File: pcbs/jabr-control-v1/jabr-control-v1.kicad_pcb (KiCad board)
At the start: 6 copper layers, 70 x 80 mm, 129 parts, among them J10001 ARJM11D7-502-AB-EW2, J10002 TYPE-C-31-M-12, J4001 MDT275E01001, J401 U.FL-R-SMT-K_895, J402 U.FL-R-SMT-K_895, J6001 MSPE-J2L0-x00, J9001 43045-0201, Q2602 DMN21D2UFB-7B, U1201 TPS259472ARPWR, U1301 MAX20004AFOC/VY+T, U2401 PESD4USB3BTTS-QX, U2402 PESD4USB3BTTS-QX, U3001 PI7C9X2G303EL, U301 TVS3301DRBR, U302 TPS26600RHFR, U3801 TPS62290TDRVRQ1, U401 LMQ66430MC3RXBRQ1, U402 TPS7B8133QDRVRQ1, U403 TPS2116DRL, U5001 LAN7431_YXX, U7 ASEK-32.768KHZ-L-R-T, U8001 LAN8870, Y8001 XRCGB25M000F3A16R0

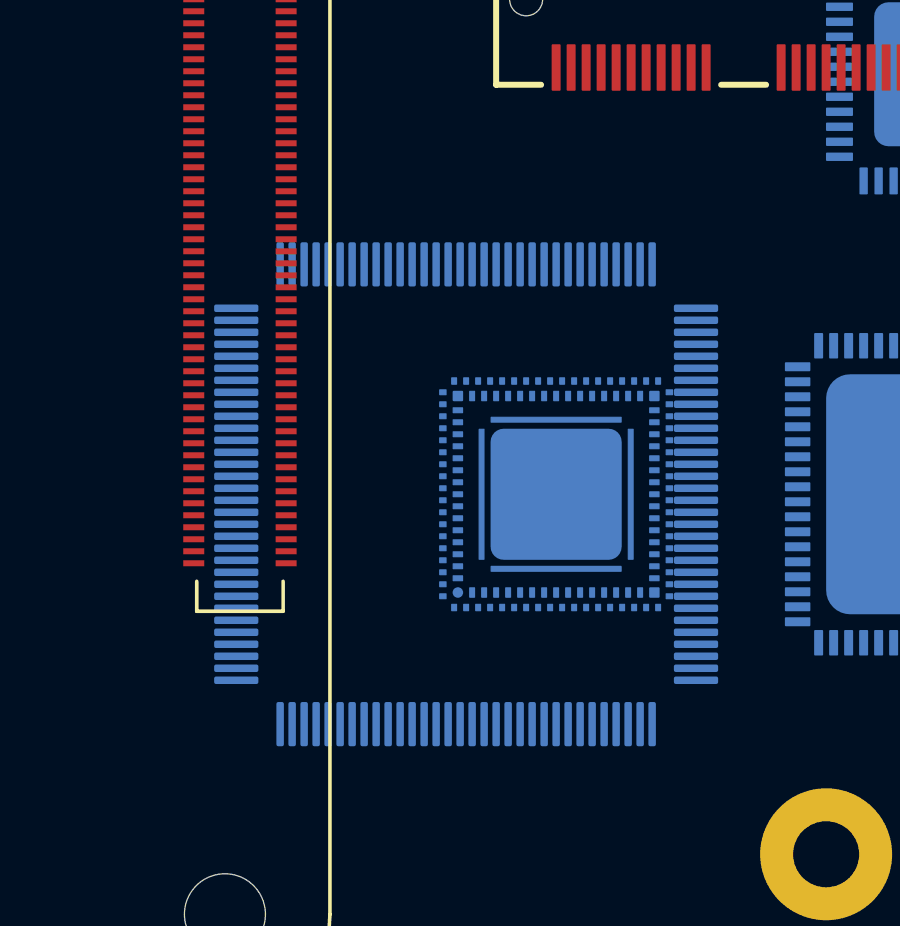
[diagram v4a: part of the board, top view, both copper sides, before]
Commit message: Changed PCIe switch to use LQFP package
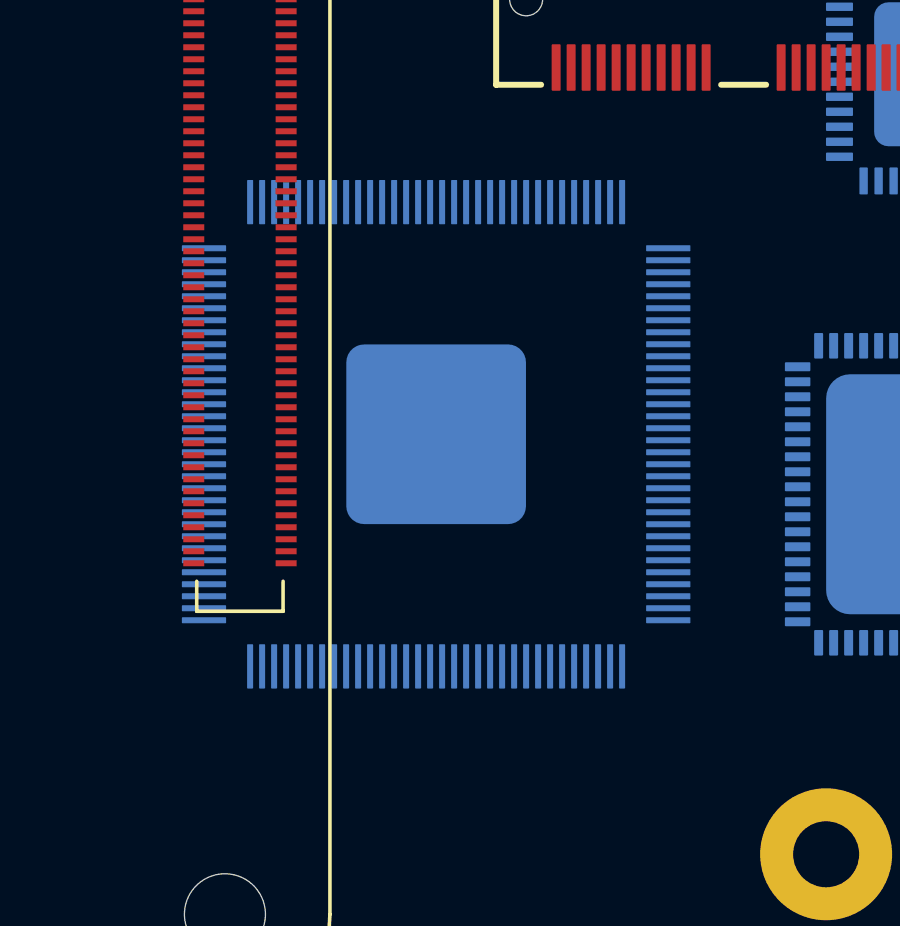
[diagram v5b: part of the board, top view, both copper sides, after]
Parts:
- removed REF**: LQFP-128_14x14mm_P0.4mm, Package_QFP:LQFP-128_14x14mm_P0.4mm
- removed U3001: PI7C9X2G303EL, project_footprints:PI7C9X2G303EL
- added U303: PI7C9X2G304SL, project_footprints:QFP40P1600X1600X160-129N, B.Cu at (173.0, 99.0)

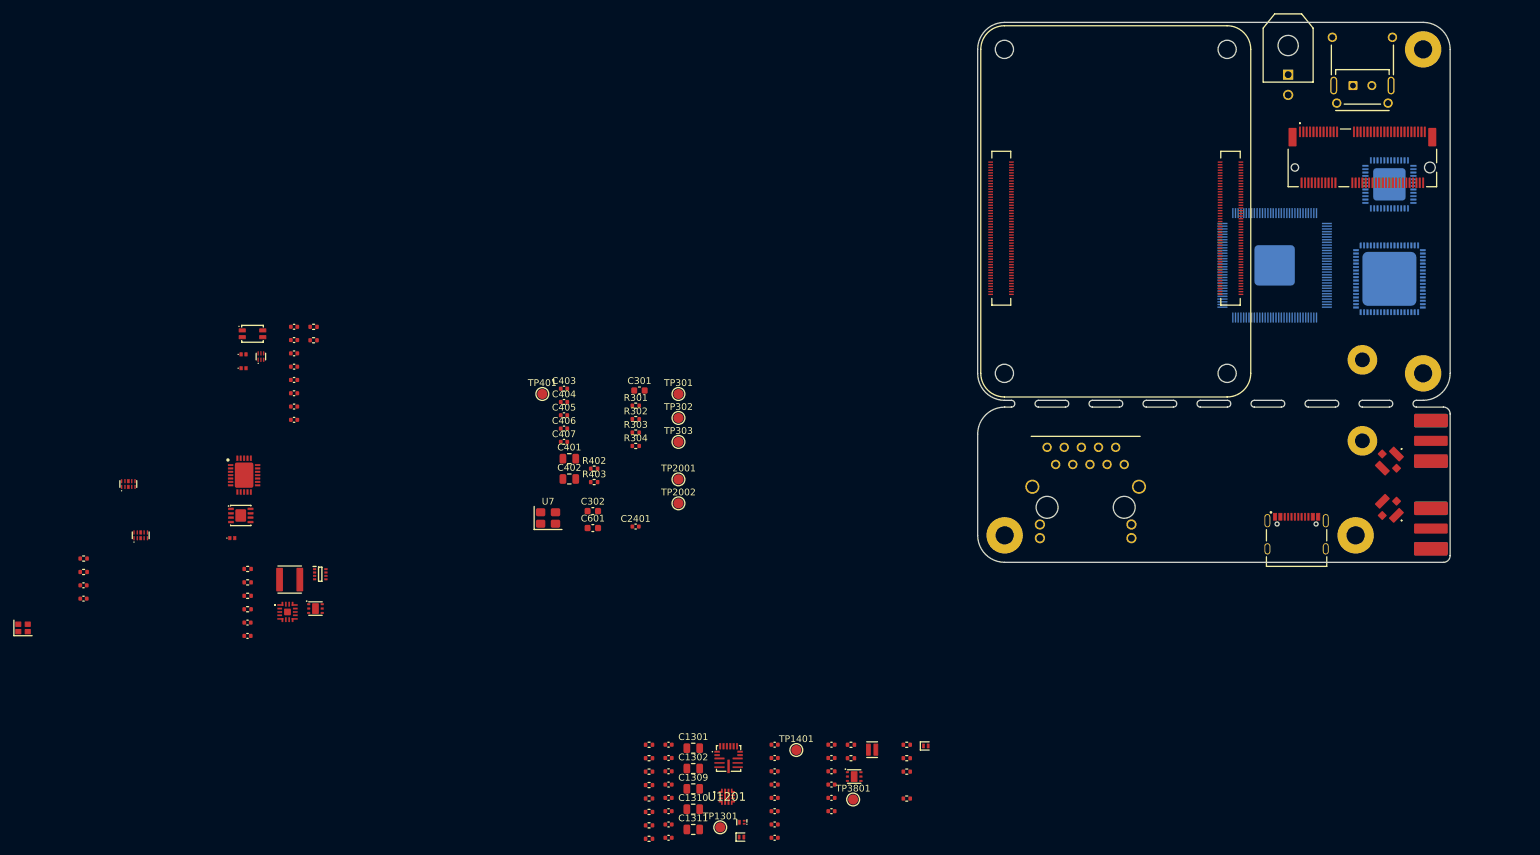
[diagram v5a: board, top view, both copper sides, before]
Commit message: Finished M.2 E-Key schematic
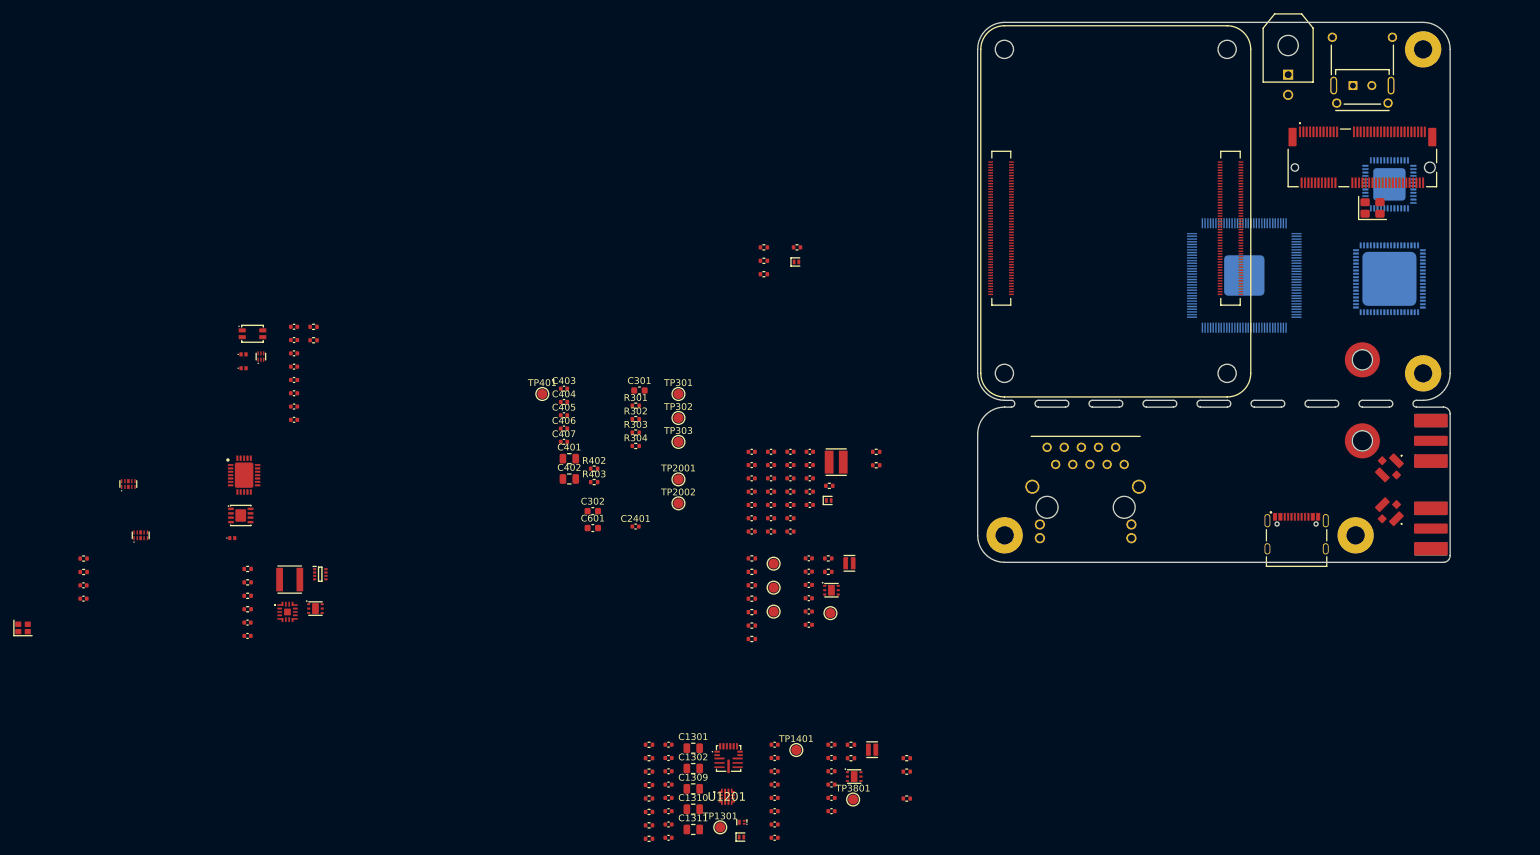
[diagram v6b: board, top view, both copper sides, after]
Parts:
- removed D202: PMEG4002EL-QYL, project_footprints:PMEG4002EL-QYL
- removed U7: ASEK-32.768KHZ-L-R-T, Crystal:Crystal_SMD_3225-4Pin_3.2x2.5mm
- added C1501: 4u7, project_footprints:C_0402, F.Cu at (104.0, 142.4)
- added C1502: 4u7, project_footprints:C_0402, F.Cu at (104.0, 144.4)
- added C1503: 22p, project_footprints:C_0402, F.Cu at (104.0, 146.3)
- added C1504: 4u7, project_footprints:C_0402, F.Cu at (104.0, 148.3)
- added C1505: 4u7, project_footprints:C_0402, F.Cu at (104.0, 150.3)
- added C1506: 4u7, project_footprints:C_0402, F.Cu at (104.0, 152.3)
- added C501: 4u7, project_footprints:C_0402, F.Cu at (95.5, 126.6)
- added C502: 1u, project_footprints:C_0402, F.Cu at (95.5, 128.6)
- added C503: 100n, project_footprints:C_0402, F.Cu at (95.5, 130.6)
- added C504: 100n, project_footprints:C_0402, F.Cu at (95.5, 132.5)
- added C505: 100n, project_footprints:C_0402, F.Cu at (95.5, 134.5)
- added C506: 100n, project_footprints:C_0402, F.Cu at (95.5, 136.5)
- added C507: 100n, project_footprints:C_0402, F.Cu at (95.5, 138.4)
- added C508: 1u, project_footprints:C_0402, F.Cu at (98.4, 126.6)
- added C509: 100n, project_footprints:C_0402, F.Cu at (98.4, 128.6)
- added C510: 100n, project_footprints:C_0402, F.Cu at (98.4, 130.6)
- added C511: 100n, project_footprints:C_0402, F.Cu at (98.4, 132.5)
- added C512: 4u7, project_footprints:C_0402, F.Cu at (98.4, 134.5)
- added C513: 4u7, project_footprints:C_0402, F.Cu at (98.4, 136.5)
- added C514: 4u7, project_footprints:C_0402, F.Cu at (98.4, 138.4)
- added C515: 4u7, project_footprints:C_0402, F.Cu at (101.3, 126.6)
- added C516: 100n, project_footprints:C_0402, F.Cu at (101.3, 128.6)
- added C517: 100n, project_footprints:C_0402, F.Cu at (101.3, 130.6)
- added C518: 100n, project_footprints:C_0402, F.Cu at (101.3, 132.5)
- added C519: 100n, project_footprints:C_0402, F.Cu at (101.3, 134.5)
- added C520: 100n, project_footprints:C_0402, F.Cu at (101.3, 136.5)
- added C521: 100n, project_footprints:C_0402, F.Cu at (101.3, 138.4)
- added C522: 100n, project_footprints:C_0402, F.Cu at (104.1, 126.6)
- added C523: 100n, project_footprints:C_0402, F.Cu at (104.1, 128.6)
- added C524: 100n, project_footprints:C_0402, F.Cu at (104.1, 130.6)
- added C525: 100n, project_footprints:C_0402, F.Cu at (104.1, 132.5)
- added C526: 100n, project_footprints:C_0402, F.Cu at (104.1, 134.5)
- added D201: PMEG4002EL-QYL, project_footprints:PMEG4002EL-QYL, F.Cu at (102.2, 98.5)
- added D501: PMEG4002EL-QYL, project_footprints:PMEG4002EL-QYL, F.Cu at (106.9, 133.8)
- added L1501: 78438313015, project_footprints:L_Wurth_WE-MAIA-1610, F.Cu at (110.0, 143.1)
- added L501: 74438333033, project_footprints:L_Wurth_WE-MAPI-3010, F.Cu at (108.0, 128.2)
- added R1501: 120k, project_footprints:R_0402, F.Cu at (106.9, 142.4)
- added R1502: 180k, project_footprints:R_0402, F.Cu at (106.9, 144.4)
- added R3001: 5k1, project_footprints:R_0402, F.Cu at (114.0, 126.6)
- added R3002: 5k1, project_footprints:R_0402, F.Cu at (114.0, 128.6)
- added R404: 10k, project_footprints:R_0402, F.Cu at (97.3, 96.3)
- added R405: 10k, project_footprints:R_0402, F.Cu at (97.3, 98.3)
- added R406: 10k, project_footprints:R_0402, F.Cu at (97.3, 100.3)
- added R501: 10k, project_footprints:R_0402, F.Cu at (107.0, 131.7)
- added R803: 10k, project_footprints:R_0402, F.Cu at (95.5, 142.4)
- added R804: 10k, project_footprints:R_0402, F.Cu at (95.5, 144.4)
- added R805: 10k, project_footprints:R_0402, F.Cu at (95.5, 146.4)
- added R806: 10k, project_footprints:R_0402, F.Cu at (95.5, 148.4)
- added R807: 10k, project_footprints:R_0402, F.Cu at (95.5, 150.4)
- added R808: 10k, project_footprints:R_0402, F.Cu at (95.5, 152.4)
- added R809: 10k, project_footprints:R_0402, F.Cu at (95.5, 154.4)
- added TP1501: 1.5mm, TestPoint:TestPoint_Pad_D1.5mm, F.Cu at (107.2, 150.5)
- added TP8001: 1.5mm, TestPoint:TestPoint_Pad_D1.5mm, F.Cu at (98.8, 146.8)
- added TP8002: 1.5mm, TestPoint:TestPoint_Pad_D1.5mm, F.Cu at (98.8, 150.3)
- added TP801: 1.5mm, TestPoint:TestPoint_Pad_D1.5mm, F.Cu at (98.8, 143.2)
- added U1501: TPS62290TDRVRQ1, project_footprints:SON65P200X200X80-7N, F.Cu at (107.3, 147.1)
- added Y401: ASEK-32.768KHZ-LRT, project_footprints:Crystal_SMD_3225-4Pin_3.2x2.5mm, F.Cu at (187.5, 90.5)
- H4001, H4002: value MountingHole_Pad -> 9774015243R; footprint MountingHole:MountingHole_2.2mm_M2_Pad -> project_footprints:9774025243R
- J4001: value MDT275E01001 -> MDT320E0X001; footprint project_footprints:MDT275E01001 -> project_footprints:MDT420E0X001
- moved R201 75.5 mm to (102.2, 96.3)
- moved U303 4.74 mm to (168.5, 100.5)
- moved J401 1.00 mm to (190.0, 129.0)
- moved J402 0.50 mm to (190.0, 135.5)
- turned H4001 to 0 degrees
- turned H4002 to 0 degrees
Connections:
- net /Power/1V1 Regulator/FB renamed /Power/1V0 & 1V1 Regulators/FB
- net /Power/1V1 Regulator/SW renamed /Power/1V0 & 1V1 Regulators/SW
- C3801 pad 1: /Power/1V1 Regulator/VIN -> +5V
- C3801 pad 2: GND1 -> GND
- C3802 pad 1: /Power/1V1 Regulator/VIN -> +5V
- C3802 pad 2: GND1 -> GND
- C3804 pad 1: /Power/1V1 Regulator/VOUT -> +1V1
- C3805 pad 1: /Power/1V1 Regulator/VOUT -> +1V1
- C3805 pad 2: GND1 -> GND
- C3806 pad 1: /Power/1V1 Regulator/VOUT -> +1V1
- C3806 pad 2: GND1 -> GND
- C3807 pad 1: /Power/1V1 Regulator/VOUT -> +1V1
- C3807 pad 2: GND1 -> GND
- H101 pad 1: SHIELD -> unconnected-(H101-Pad1)
- H102 pad 1: SHIELD -> unconnected-(H102-Pad1)
- H103 pad 1: SHIELD -> unconnected-(H103-Pad1)
- H105 pad 1: SHIELD -> unconnected-(H105-Pad1)
- J4001 pad 11: unconnected-(J4001-SDIO_CMD-Pad11) -> /M.2 E-Key/MOSI
- J4001 pad 13: unconnected-(J4001-SDIO_DATA0-Pad13) -> /M.2 E-Key/MISO
- J4001 pad 15: unconnected-(J4001-SDIO_DATA1-Pad15) -> /M.2 E-Key/~{SPI_INT}
- J4001 pad 19: unconnected-(J4001-SDIO_DATA3-Pad19) -> /M.2 E-Key/CS
- J4001 pad 22: unconnected-(J4001-UART_RXD-Pad22) -> /M.2 E-Key/TX
- J4001 pad 23: unconnected-(J4001-~{SDIO_RESET}-Pad23) -> /CM5/~{RST_3V3}
- J4001 pad 32: unconnected-(J4001-UART_TXD-Pad32) -> /M.2 E-Key/RX
- J4001 pad 50: unconnected-(J4001-SUSCLK-Pad50) -> /M.2 E-Key/SUSCLK
- J4001 pad 54: unconnected-(J4001-~{W_DISABLE2}-Pad54) -> /CM5/~{BT_DISABLE}
- J4001 pad 56: unconnected-(J4001-~{W_DISABLE1}-Pad56) -> /CM5/~{WL_DISABLE}
- J4001 pad 58: unconnected-(J4001-I2C_DATA-Pad58) -> /CM5/I2C2.SDA
- J4001 pad 60: unconnected-(J4001-I2C_CLK-Pad60) -> /CM5/I2C2.SCL
- J4001 pad 62: unconnected-(J4001-~{ALERT}-Pad62) -> /M.2 E-Key/~{I2C_INT}
- J4001 pad 9: unconnected-(J4001-SDIO_CLK-Pad9) -> /M.2 E-Key/CLK
- L3801 pad 2: /Power/1V1 Regulator/VOUT -> +1V1
- R201 pad 2: /CM5/~{RST} -> /CM5/~{RST_3V3}
- R203 pad 2: /CM5/~{LED_PWR_A} -> /CM5/~{LED_ACT_A}
- R204 pad 2: /CM5/~{LED_PWR_K} -> /CM5/~{LED_PWR_A}
- R3801 pad 1: /Power/1V1 Regulator/VOUT -> +1V1
- R3802 pad 2: GND1 -> GND
- R5003 pad 1: +3V3 -> +1V8
- R5004 pad 1: +3V3 -> +1V8
- R5005 pad 1: +3V3_AON -> /PCIe to 1000BASE-T1/PCIe MAC/VAUX_DET
- R5005 pad 2: /PCIe to 1000BASE-T1/PCIe MAC/VAUX_DET -> GND
- R8002 pad 1: unconnected-(R8002-Pad1) -> +1V8
- SOM2001 pad 78: unconnected-(SOM2001D-VREF-Pad78) -> +3V3
- SOM2001 pad 89: unconnected-(SOM2001D-WIFI_EN-Pad89) -> /CM5/~{WL_DISABLE}
- SOM2001 pad 91: unconnected-(SOM2001D-BT_EN-Pad91) -> /CM5/~{BT_DISABLE}
- SOM2001 pad 92: /CM5/PWR_BUT -> /CM5/~{RST_5V}
- TP3801 pad 1: /Power/1V1 Regulator/VOUT -> +1V1
- U303 pad 1: Net-(U303C-VDDR-Pad1) -> +3V3
- U303 pad 105: Net-(U303C-AVDD-Pad105) -> +1V0
- U303 pad 108: Net-(U303C-AVDD-Pad105) -> +1V0
- U303 pad 11: unconnected-(U303C-VSS-Pad11) -> GND
- U303 pad 113: unconnected-(U303C-AVDDH-Pad113) -> +3V3
- U303 pad 119: Net-(U303C-AVDD-Pad105) -> +1V0
- U303 pad 125: Net-(U303C-AVDD-Pad105) -> +1V0
- U303 pad 13: Net-(U303C-VDDCAUX-Pad13) -> +1V0
- U303 pad 14: Net-(U303C-VDDCAUX-Pad13) -> +1V0
- U303 pad 15: unconnected-(U303C-VAUX-Pad15) -> +3V3
- U303 pad 23: Net-(U303C-VDDC-Pad23) -> +1V0
- U303 pad 26: unconnected-(U303B-SMBCLK-Pad26) -> /CM5/I2C2.SCL
- U303 pad 27: unconnected-(U303B-SMBDATA-Pad27) -> /CM5/I2C2.SDA
- U303 pad 29: Net-(U303C-VDDC-Pad23) -> +1V0
- U303 pad 3: Net-(U303C-VDDC-Pad23) -> +1V0
- U303 pad 31: Net-(U303C-VDDC-Pad23) -> +1V0
- U303 pad 40: Net-(U303C-VDDC-Pad23) -> +1V0
- U303 pad 42: unconnected-(U303B-GPIO5-Pad42) -> GND
- U303 pad 43: unconnected-(U303B-GPIO6-Pad43) -> GND
- U303 pad 44: unconnected-(U303B-GPIO7-Pad44) -> GND
- U303 pad 49: Net-(U303C-VDDR-Pad1) -> +3V3
- U303 pad 55: Net-(U303C-VDDC-Pad23) -> +1V0
- U303 pad 62: Net-(U303C-VDDC-Pad23) -> +1V0
- U303 pad 64: Net-(U303C-VDDR-Pad1) -> +3V3
- U303 pad 65: Net-(U303C-VDDC-Pad23) -> +1V0
- U303 pad 79: Net-(U303C-CVDDR-Pad79) -> +3V3
- U303 pad 8: Net-(U303C-VDDR-Pad1) -> +3V3
- U303 pad 82: Net-(U303C-CVDDR-Pad79) -> +3V3
- U303 pad 84: Net-(U303C-CVDDR-Pad79) -> +3V3
- U303 pad 91: Net-(U303C-VDDC-Pad23) -> +1V0
- U303 pad 96: Net-(U303C-VDDR-Pad1) -> +3V3
- U303 pad 99: Net-(U303C-AVDD-Pad105) -> +1V0
- U3801 pad 2: GND1 -> GND
- U3801 pad 4: /Power/1V1 Regulator/VIN -> +5V
- U3801 pad 5: /Power/1V1 Regulator/VIN -> +5V
- U3801 pad 6: GND1 -> GND
- U3801 pad 7: GND1 -> GND
- U5001 pad 1: Net-(U5001A-AVDDH_1) -> +2V5
- U5001 pad 12: +3V3 -> +1V8
- U5001 pad 19: +3V3 -> +1V8
- U5001 pad 2: Net-(U5001A-AVDD12) -> +1V2
- U5001 pad 24: Net-(U5001A-AVDD12) -> +1V2
- U5001 pad 25: Net-(U5001A-AVDD12) -> +1V2
- U5001 pad 3: +3V3 -> +1V8
- U5001 pad 31: Net-(U5001A-AVDD12) -> +1V2
- U5001 pad 34: Net-(U5001A-AVDDH_1) -> +2V5
- U5001 pad 38: unconnected-(U5001A-VDD25_REG_OUT-Pad38) -> +2V5
- U5001 pad 39: unconnected-(U5001A-VDD_REG_IN-Pad39) -> +3V3
- U5001 pad 40: +3V3 -> +1V8
- U5001 pad 43: +3V3 -> +1V8
- U5001 pad 44: /CM5/~{RST} -> Net-(D501-A)
- U5001 pad 46: Net-(U5001A-AVDD12) -> +1V2
- U5001 pad 48: +3V3 -> +1V8
- U5001 pad 51: unconnected-(U5001A-VDD12_SW_OUT-Pad51) -> /PCIe to 1000BASE-T1/PCIe MAC/SW
- U5001 pad 52: unconnected-(U5001A-VDD_SW_IN-Pad52) -> +1V8
- U5001 pad 53: unconnected-(U5001A-VDD12_SW_FB-Pad53) -> +1V2
- U5001 pad 61: +3V3 -> +1V8
- U5001 pad 62: Net-(U5001A-AVDD12) -> +1V2
- U5001 pad 69: Net-(U5001A-AVDD12) -> +1V2
- U5001 pad 7: +3V3 -> +1V8
- U8001 pad 13: Net-(U8001B-VDDIO) -> +1V8
- U8001 pad 18: unconnected-(U8001A-1588_EVT/MODE_STRP-Pad18) -> /PCIe to 1000BASE-T1/1000BASE-T1 PHY/MODE
- U8001 pad 20: Net-(U8001B-VDDIO) -> +1V8
- U8001 pad 22: unconnected-(U8001B-S_VP-Pad22) -> /PCIe to 1000BASE-T1/1000BASE-T1 PHY/S_VP
- U8001 pad 3: unconnected-(U8001A-WAKE_IN-Pad3) -> GND
- U8001 pad 36: Net-(U8001B-VDDIO) -> +1V8
- U8001 pad 38: unconnected-(U8001A-LED1/GPIO1-Pad38) -> /PCIe to 1000BASE-T1/1000BASE-T1 PHY/1588_CLK_ADJ
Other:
- board text added: "Max component height on M.2 module is 1.5mm per side. 4.2mm High M.2 connector gives 2.54mm clearance between boards. Therefore component heights under the M.2 slot should be kept under 1mm where possible."
